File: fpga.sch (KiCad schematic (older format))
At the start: 12 parts

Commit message: initial footprint assignment and VERY rough placement
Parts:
- C301, C302, C303, C304, C305, C306, C307, C308: renamed from C?; footprint (none) -> Capacitor_SMD:C_0402_1005Metric
- gave numbers to parts that had none: 1
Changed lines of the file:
@@
 $EndDescr
 $Comp
-L FPGA_Lattice:ICE40HX1K-TQ144 U?
+L FPGA_Lattice:ICE40HX1K-TQ144 U301
 U 1 1 5E13ADC3
 P 2650 2750
-F 0 "U?" H 2300 4050 50  0000 L CNN
+F 0 "U301" H 2300 4050 50  0000 L CNN
 F 1 "ICE40HX1K-TQ144" H 2300 1450 50  0000 L CNN
 F 2 "Package_QFP:TQFP-144_20x20mm_P0.5mm" H 2650 1300 50  0001 C CNN
@@
 $EndComp
 $Comp
-L FPGA_Lattice:ICE40HX1K-TQ144 U?
+L FPGA_Lattice:ICE40HX1K-TQ144 U301
 U 2 1 5E142A3F
 P 4850 2850
-F 0 "U?" H 4500 4250 50  0000 L CNN
+F 0 "U301" H 4500 4250 50  0000 L CNN
 F 1 "ICE40HX1K-TQ144" H 4500 1450 50  0000 L CNN
 F 2 "Package_QFP:TQFP-144_20x20mm_P0.5mm" H 4850 1400 50  0001 C CNN
@@
 $EndComp
 $Comp
-L FPGA_Lattice:ICE40HX1K-TQ144 U?
+L FPGA_Lattice:ICE40HX1K-TQ144 U301
 U 3 1 5E145C74
 P 6850 2650
-F 0 "U?" H 6500 3850 50  0000 L CNN
+F 0 "U301" H 6500 3850 50  0000 L CNN
 F 1 "ICE40HX1K-TQ144" H 6500 1450 50  0000 L CNN
 F 2 "Package_QFP:TQFP-144_20x20mm_P0.5mm" H 6850 1200 50  0001 C CNN
@@
 $EndComp
 $Comp
-L FPGA_Lattice:ICE40HX1K-TQ144 U?
+L FPGA_Lattice:ICE40HX1K-TQ144 U301
 U 4 1 5E14AAA8
 P 8850 2850
-F 0 "U?" H 8500 4250 50  0000 L CNN
+F 0 "U301" H 8500 4250 50  0000 L CNN
 F 1 "ICE40HX1K-TQ144" H 8500 1450 50  0000 L CNN
 F 2 "Package_QFP:TQFP-144_20x20mm_P0.5mm" H 8850 1400 50  0001 C CNN
@@
 $EndComp
 $Comp
-L Device:C C?
+L Device:C C301
 U 1 1 5E121210
 P 3100 1150
-F 0 "C?" H 3215 1196 50  0000 L CNN
+F 0 "C301" H 3215 1196 50  0000 L CNN
 F 1 "0.1u" H 3215 1105 50  0000 L CNN
-F 2 "" H 3138 1000 50  0001 C CNN
+F 2 "Capacitor_SMD:C_0402_1005Metric" H 3138 1000 50  0001 C CNN
 F 3 "~" H 3100 1150 50  0001 C CNN
 	1    3100 1150
@@
 $EndComp
 $Comp
-L Device:C C?
+L Device:C C302
 U 1 1 5E121216
 P 3500 1150
-F 0 "C?" H 3615 1196 50  0000 L CNN
+F 0 "C302" H 3615 1196 50  0000 L CNN
 F 1 "0.1u" H 3615 1105 50  0000 L CNN
-F 2 "" H 3538 1000 50  0001 C CNN
+F 2 "Capacitor_SMD:C_0402_1005Metric" H 3538 1000 50  0001 C CNN
 F 3 "~" H 3500 1150 50  0001 C CNN
 	1    3500 1150
@@
 	3500 1500 3500 1400
 $Comp
-L power:GND #PWR?
+L power:GND #PWR0301
 U 1 1 5E121226
 P 3500 1500
-F 0 "#PWR?" H 3500 1250 50  0001 C CNN
+F 0 "#PWR0301" H 3500 1250 50  0001 C CNN
 F 1 "GND" H 3505 1327 50  0000 C CNN
 F 2 "" H 3500 1500 50  0001 C CNN
@@
 Connection ~ 3500 1400
 $Comp
-L Device:C C?
+L Device:C C303
 U 1 1 5E122A60
 P 5300 1150
-F 0 "C?" H 5415 1196 50  0000 L CNN
+F 0 "C303" H 5415 1196 50  0000 L CNN
 F 1 "0.1u" H 5415 1105 50  0000 L CNN
-F 2 "" H 5338 1000 50  0001 C CNN
+F 2 "Capacitor_SMD:C_0402_1005Metric" H 5338 1000 50  0001 C CNN
 F 3 "~" H 5300 1150 50  0001 C CNN
 	1    5300 1150
@@
 $EndComp
 $Comp
-L Device:C C?
+L Device:C C304
 U 1 1 5E122A66
 P 5700 1150
-F 0 "C?" H 5815 1196 50  0000 L CNN
+F 0 "C304" H 5815 1196 50  0000 L CNN
 F 1 "0.1u" H 5815 1105 50  0000 L CNN
-F 2 "" H 5738 1000 50  0001 C CNN
+F 2 "Capacitor_SMD:C_0402_1005Metric" H 5738 1000 50  0001 C CNN
 F 3 "~" H 5700 1150 50  0001 C CNN
 	1    5700 1150
@@
 	5700 1500 5700 1400
 $Comp
-L power:GND #PWR?
+L power:GND #PWR0302
 U 1 1 5E122A76
 P 5700 1500
-F 0 "#PWR?" H 5700 1250 50  0001 C CNN
+F 0 "#PWR0302" H 5700 1250 50  0001 C CNN
 F 1 "GND" H 5705 1327 50  0000 C CNN
 F 2 "" H 5700 1500 50  0001 C CNN
@@
 Connection ~ 5700 1400
 $Comp
-L Device:C C?
+L Device:C C305
 U 1 1 5E1239E6
 P 7300 1150
-F 0 "C?" H 7415 1196 50  0000 L CNN
+F 0 "C305" H 7415 1196 50  0000 L CNN
 F 1 "0.1u" H 7415 1105 50  0000 L CNN
-F 2 "" H 7338 1000 50  0001 C CNN
+F 2 "Capacitor_SMD:C_0402_1005Metric" H 7338 1000 50  0001 C CNN
 F 3 "~" H 7300 1150 50  0001 C CNN
 	1    7300 1150
@@
 $EndComp
 $Comp
-L Device:C C?
+L Device:C C306
 U 1 1 5E1239EC
 P 7700 1150
-F 0 "C?" H 7815 1196 50  0000 L CNN
+F 0 "C306" H 7815 1196 50  0000 L CNN
 F 1 "0.1u" H 7815 1105 50  0000 L CNN
-F 2 "" H 7738 1000 50  0001 C CNN
+F 2 "Capacitor_SMD:C_0402_1005Metric" H 7738 1000 50  0001 C CNN
 F 3 "~" H 7700 1150 50  0001 C CNN
 	1    7700 1150
@@
 	7700 1500 7700 1400
 $Comp
-L power:GND #PWR?
+L power:GND #PWR0303
 U 1 1 5E1239FC
 P 7700 1500
-F 0 "#PWR?" H 7700 1250 50  0001 C CNN
+F 0 "#PWR0303" H 7700 1250 50  0001 C CNN
 F 1 "GND" H 7705 1327 50  0000 C CNN
 F 2 "" H 7700 1500 50  0001 C CNN
@@
 Connection ~ 7700 1400
 $Comp
-L Device:C C?
+L Device:C C307
 U 1 1 5E126152
 P 9300 1150
-F 0 "C?" H 9415 1196 50  0000 L CNN
+F 0 "C307" H 9415 1196 50  0000 L CNN
 F 1 "0.1u" H 9415 1105 50  0000 L CNN
-F 2 "" H 9338 1000 50  0001 C CNN
+F 2 "Capacitor_SMD:C_0402_1005Metric" H 9338 1000 50  0001 C CNN
 F 3 "~" H 9300 1150 50  0001 C CNN
 	1    9300 1150
@@
 $EndComp
 $Comp
-L Device:C C?
+L Device:C C308
 U 1 1 5E126158
 P 9700 1150
-F 0 "C?" H 9815 1196 50  0000 L CNN
+F 0 "C308" H 9815 1196 50  0000 L CNN
 F 1 "0.1u" H 9815 1105 50  0000 L CNN
-F 2 "" H 9738 1000 50  0001 C CNN
+F 2 "Capacitor_SMD:C_0402_1005Metric" H 9738 1000 50  0001 C CNN
 F 3 "~" H 9700 1150 50  0001 C CNN
 	1    9700 1150
@@
 	9700 1500 9700 1400
 $Comp
-L power:GND #PWR?
+L power:GND #PWR0304
 U 1 1 5E126168
 P 9700 1500
-F 0 "#PWR?" H 9700 1250 50  0001 C CNN
+F 0 "#PWR0304" H 9700 1250 50  0001 C CNN
 F 1 "GND" H 9705 1327 50  0000 C CNN
 F 2 "" H 9700 1500 50  0001 C CNN

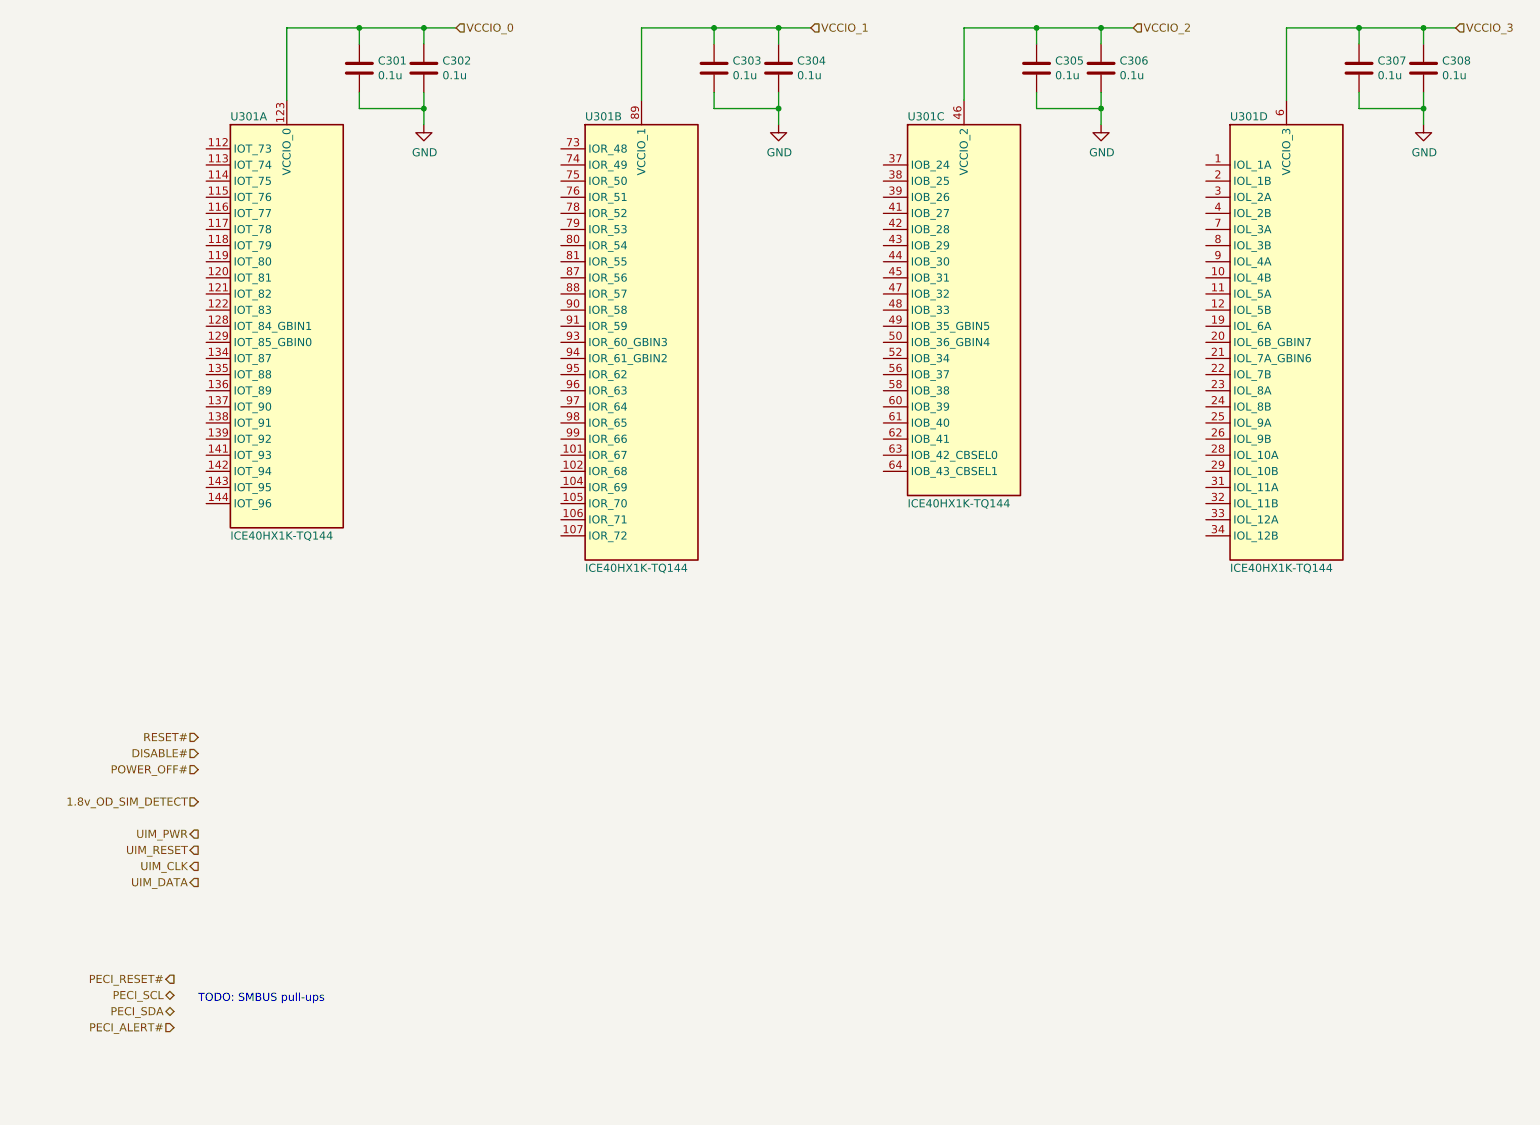
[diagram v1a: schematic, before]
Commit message: assigning pins, adding test points, placing stuff, etc
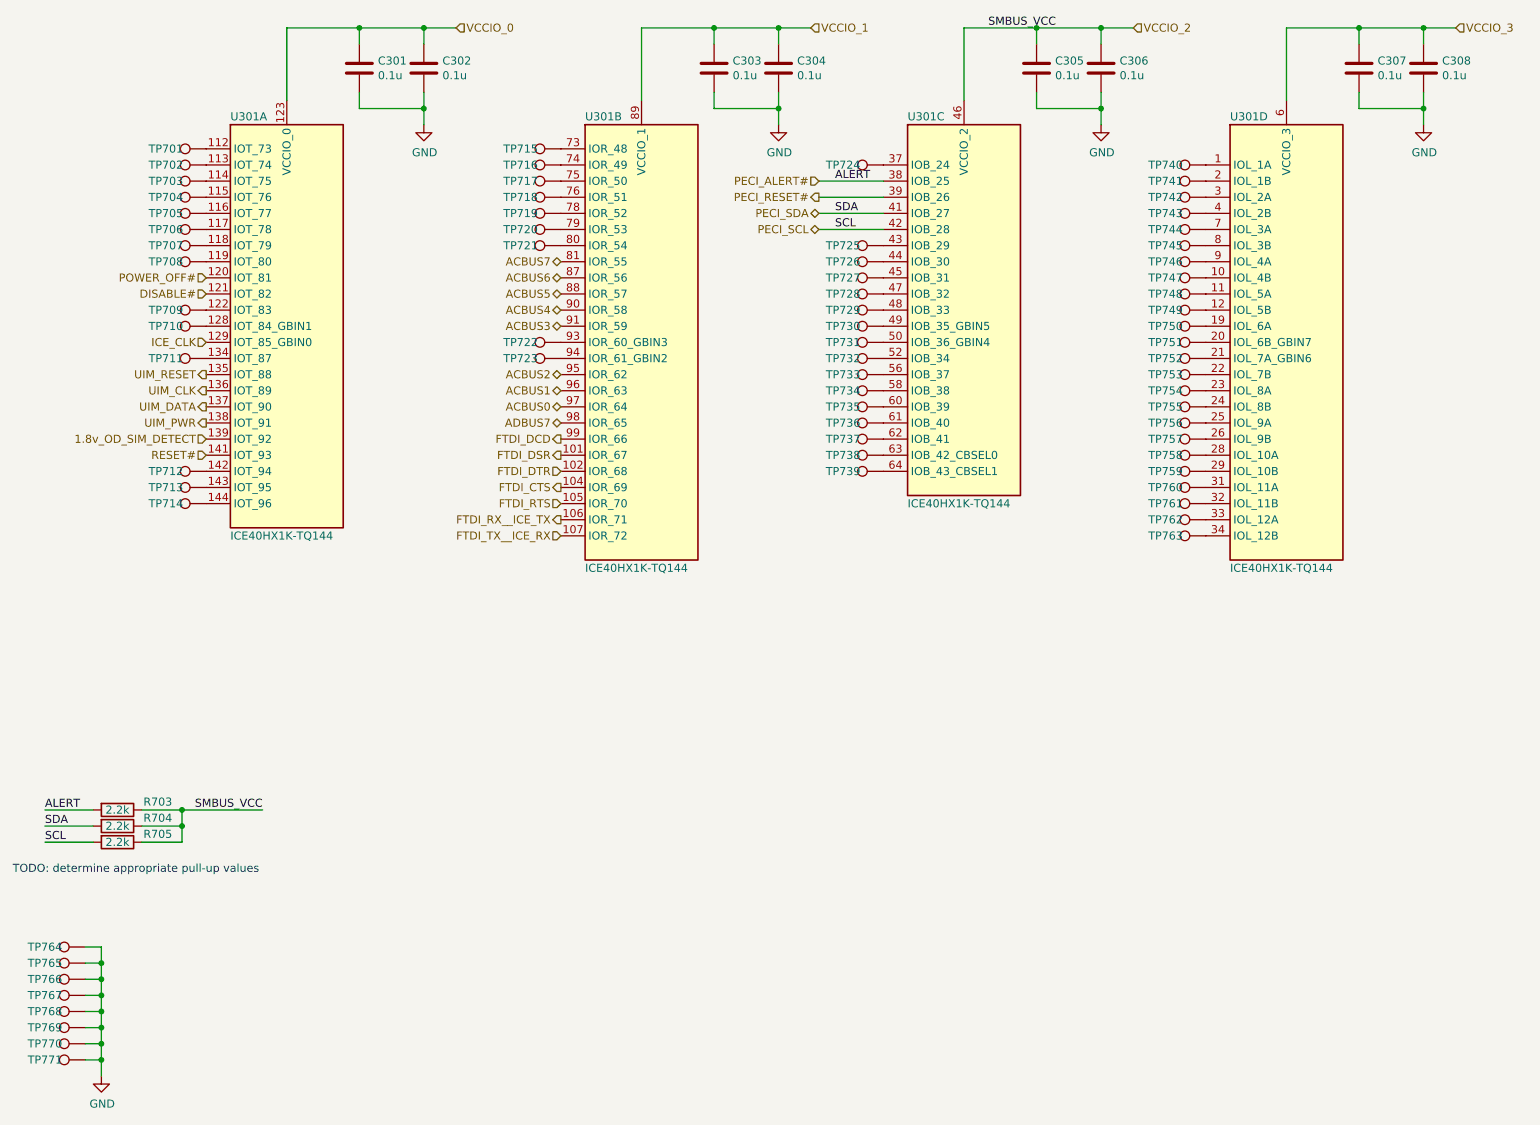
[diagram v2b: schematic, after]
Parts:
- added R703, R704, R705: 2.2k, Resistor_SMD:R_0402_1005Metric, symbol Device:R
- added TP701, TP702, TP703, TP704, TP705, TP706, TP707, TP708, TP709, TP710, TP711, TP712, TP713, TP714, TP715, TP716, TP717, TP718, TP719, TP720, TP721, TP722, TP723, TP724, TP725, TP726, TP727, TP728, TP729, TP730, TP731, TP732, TP733, TP734, TP735, TP736, TP737, TP738, TP739, TP740, TP741, TP742, TP743, TP744, TP745, TP746, TP747, TP748, TP749, TP750, TP751, TP752, TP753, TP754, TP755, TP756, TP757, TP758, TP759, TP760, TP761, TP762, TP763, TP764, TP765, TP766, TP767, TP768, TP769, TP770, TP771: TestPoint, m2-ice40:TestPoint_Pad_0.5x1.5mm, symbol Connector:TestPoint
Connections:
- net 1.8v_OD_SIM_DETECT: now also U301.139 (IOT_92)
- net DISABLE#: now also U301.121 (IOT_82)
- net GND: now also TP764.1, TP765.1, TP766.1, TP767.1, TP768.1, TP769.1, TP770.1, TP771.1
- net PECI_ALERT#: now also U301.38 (IOB_25), R703.2
- net PECI_RESET#: now also U301.39 (IOB_26)
- net PECI_SCL: now also U301.42 (IOB_28), R705.2
- net PECI_SDA: now also U301.41 (IOB_27), R704.2
- net POWER_OFF#: now also U301.120 (IOT_81)
- net RESET#: now also U301.141 (IOT_93)
- net UIM_CLK: now also U301.136 (IOT_89)
- net UIM_DATA: now also U301.137 (IOT_90)
- net UIM_PWR: now also U301.138 (IOT_91)
- net UIM_RESET: now also U301.135 (IOT_88)
- net VCCIO_2: now also R703.1, R704.1, R705.1
- net at U301.112 (IOT_73): now also TP701.1
- net at U301.113 (IOT_74): now also TP702.1
- net at U301.114 (IOT_75): now also TP703.1
- net at U301.115 (IOT_76): now also TP704.1
- net at U301.116 (IOT_77): now also TP705.1
- net at U301.117 (IOT_78): now also TP706.1
- net at U301.118 (IOT_79): now also TP707.1
- net at U301.119 (IOT_80): now also TP708.1
- net at U301.122 (IOT_83): now also TP709.1
- net at U301.128 (IOT_84_GBIN1): now also TP710.1
- net ICE_CLK: now reaches U301.129 (IOT_85_GBIN0)
- net at U301.134 (IOT_87): now also TP711.1
- net at U301.142 (IOT_94): now also TP712.1
- net at U301.143 (IOT_95): now also TP713.1
- net at U301.144 (IOT_96): now also TP714.1
- net FTDI_DSR: now reaches U301.101 (IOR_67)
- net FTDI_DTR: now reaches U301.102 (IOR_68)
- net FTDI_CTS: now reaches U301.104 (IOR_69)
- net FTDI_RTS: now reaches U301.105 (IOR_70)
- net FTDI_RX__ICE_TX: now reaches U301.106 (IOR_71)
- net FTDI_TX__ICE_RX: now reaches U301.107 (IOR_72)
- net at U301.73 (IOR_48): now also TP715.1
- net at U301.74 (IOR_49): now also TP716.1
- net at U301.75 (IOR_50): now also TP717.1
- net at U301.76 (IOR_51): now also TP718.1
- net at U301.78 (IOR_52): now also TP719.1
- net at U301.79 (IOR_53): now also TP720.1
- net at U301.80 (IOR_54): now also TP721.1
- net ACBUS7: now reaches U301.81 (IOR_55)
- net ACBUS6: now reaches U301.87 (IOR_56)
- net ACBUS5: now reaches U301.88 (IOR_57)
- net ACBUS4: now reaches U301.90 (IOR_58)
- net ACBUS3: now reaches U301.91 (IOR_59)
- net at U301.93 (IOR_60_GBIN3): now also TP722.1
- net at U301.94 (IOR_61_GBIN2): now also TP723.1
- net ACBUS2: now reaches U301.95 (IOR_62)
- net ACBUS1: now reaches U301.96 (IOR_63)
- net ACBUS0: now reaches U301.97 (IOR_64)
- net ADBUS7: now reaches U301.98 (IOR_65)
- net FTDI_DCD: now reaches U301.99 (IOR_66)
- net at U301.37 (IOB_24): now also TP724.1
- net at U301.43 (IOB_29): now also TP725.1
- net at U301.44 (IOB_30): now also TP726.1
- net at U301.45 (IOB_31): now also TP727.1
- net at U301.47 (IOB_32): now also TP728.1
- net at U301.48 (IOB_33): now also TP729.1
- net at U301.49 (IOB_35_GBIN5): now also TP730.1
- net at U301.50 (IOB_36_GBIN4): now also TP731.1
- net at U301.52 (IOB_34): now also TP732.1
- net at U301.56 (IOB_37): now also TP733.1
- net at U301.58 (IOB_38): now also TP734.1
- net at U301.60 (IOB_39): now also TP735.1
- net at U301.61 (IOB_40): now also TP736.1
- net at U301.62 (IOB_41): now also TP737.1
- net at U301.63 (IOB_42_CBSEL0): now also TP738.1
- net at U301.64 (IOB_43_CBSEL1): now also TP739.1
- net at U301.1 (IOL_1A): now also TP740.1
- net at U301.10 (IOL_4B): now also TP747.1
- net at U301.11 (IOL_5A): now also TP748.1
- net at U301.12 (IOL_5B): now also TP749.1
- net at U301.19 (IOL_6A): now also TP750.1
- net at U301.2 (IOL_1B): now also TP741.1
- net at U301.20 (IOL_6B_GBIN7): now also TP751.1
- net at U301.21 (IOL_7A_GBIN6): now also TP752.1
- net at U301.22 (IOL_7B): now also TP753.1
- net at U301.23 (IOL_8A): now also TP754.1
- net at U301.24 (IOL_8B): now also TP755.1
- net at U301.25 (IOL_9A): now also TP756.1
- net at U301.26 (IOL_9B): now also TP757.1
- net at U301.28 (IOL_10A): now also TP758.1
- net at U301.29 (IOL_10B): now also TP759.1
- net at U301.3 (IOL_2A): now also TP742.1
- net at U301.31 (IOL_11A): now also TP760.1
- net at U301.32 (IOL_11B): now also TP761.1
- net at U301.33 (IOL_12A): now also TP762.1
- net at U301.34 (IOL_12B): now also TP763.1
- net at U301.4 (IOL_2B): now also TP743.1
- net at U301.7 (IOL_3A): now also TP744.1
- net at U301.8 (IOL_3B): now also TP745.1
- net at U301.9 (IOL_4A): now also TP746.1
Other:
- note added: "TODO: determine appropriate pull-up values"
- note removed: "TODO: SMBUS pull-ups"
